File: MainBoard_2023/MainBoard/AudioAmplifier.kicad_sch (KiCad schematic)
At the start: 0 parts

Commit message: アンプ回路
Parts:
- added C? (x7): 1μ, symbol Device:C_Small
- added R? (x7): 10k, symbol Device:R_Small
- added R?: 100k, symbol Device:R_Small
- added U?: YDA142, symbol YDA142:YDA142
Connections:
- new net: R?.1, U?.48 (SLEEPN), U?.49 (PROTN)
- new net: C?.1, U?.1 (VREF), U?.4 (GAINA)
- new net +12V: C?.1, C?.1, C?.1, C?.2, C?.2, R?.2, U?.10 (PVDDR), U?.17 (PVDDR), U?.36 (PVDDL), U?.43 (PVDDL), U?.50 (PVDDREG)
- new net +5VD: C?.1, R?.2, R?.2, R?.2, R?.2, R?.2, R?.2, R?.2, U?.21 (MUTEN), U?.51 (REFA), U?.52 (DVDD)
- new net BCLK: U?.26 (SCLK)
- new net BITSEL: R?.1, U?.33 (BITSEL)
- new net DIN: U?.24 (SDIN)
- new net FSSEL: R?.1, U?.32 (FSSEL)
- new net GAIN0: R?.1, U?.29 (GAIN0)
- new net GAIN1: R?.1, U?.30 (GAIN1)
- new net GAIN2: R?.1, U?.31 (GAIN2)
- new net GND: C?.1, C?.1, C?.2, C?.2, C?.2, C?.2, C?.2, U?.13 (PVSSR), U?.14 (PVSSR), U?.18 (PVSSR), U?.19 (PVSSR), U?.2 (AVSS), U?.22 (MONO), U?.23 (DVSS), U?.3 (VSSBGR), U?.34 (PVSSL), U?.35 (PVSSL), U?.39 (PVSSL), U?.40 (PVSSL), U?.44 (PVSSL), U?.45 (PVSSL), U?.8 (PVSSR), U?.9 (PVSSR)
- new net LRCLK: U?.25 (LRCLK)
- new net MODE0: R?.1, U?.27 (MODE0)
- new net MODE1: R?.1, U?.28 (MODE1)
- new net SP_OUTM_L: U?.37 (OUTML), U?.38 (OUTML)
- new net SP_OUTM_R: U?.15 (OUTMR), U?.16 (OUTMR)
- new net SP_OUTP_L: U?.41 (OUTPL), U?.42 (OUTPL)
- new net SP_OUTP_R: U?.11 (OUTPR), U?.12 (OUTPR)
- no-connect marks 0 -> 6

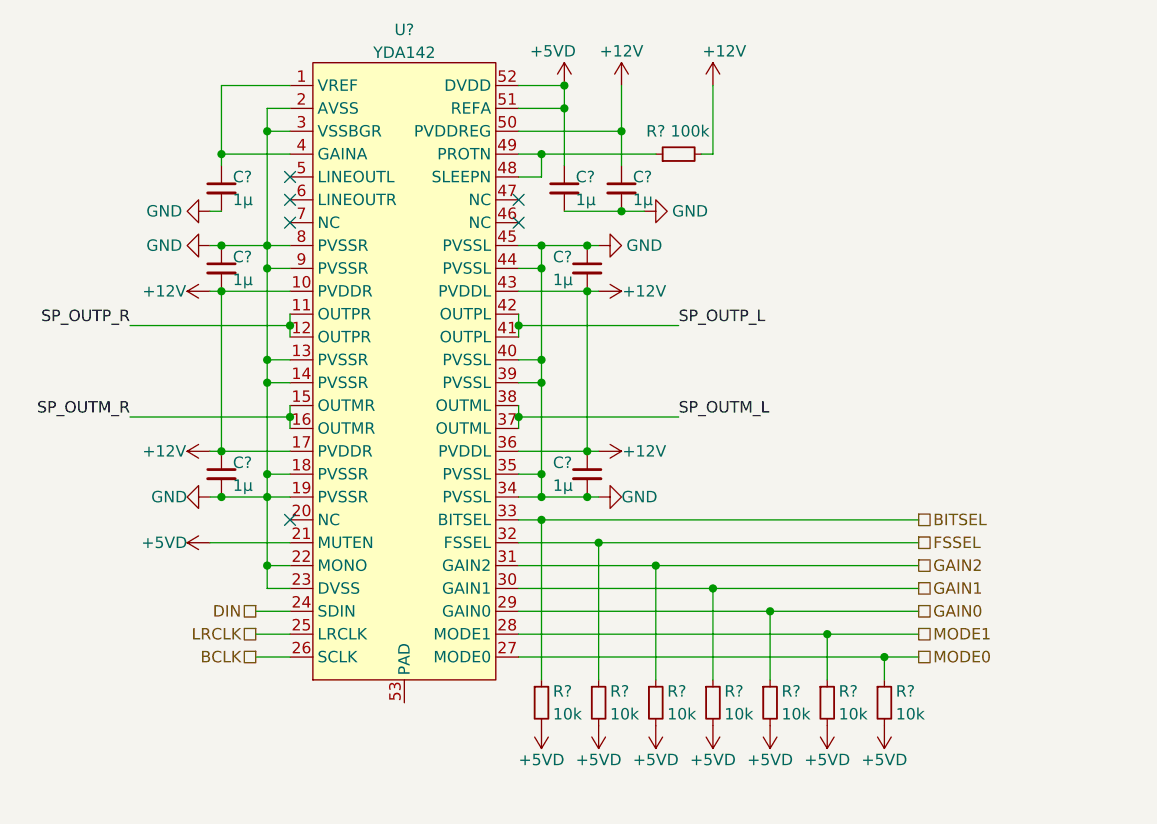
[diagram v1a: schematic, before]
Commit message: 回路だいたい完成
電解コンデンサのシンボルとフットプリントをkicad付属のものにする
ADCのピンと、SPIのOLEDのピンを共用にする
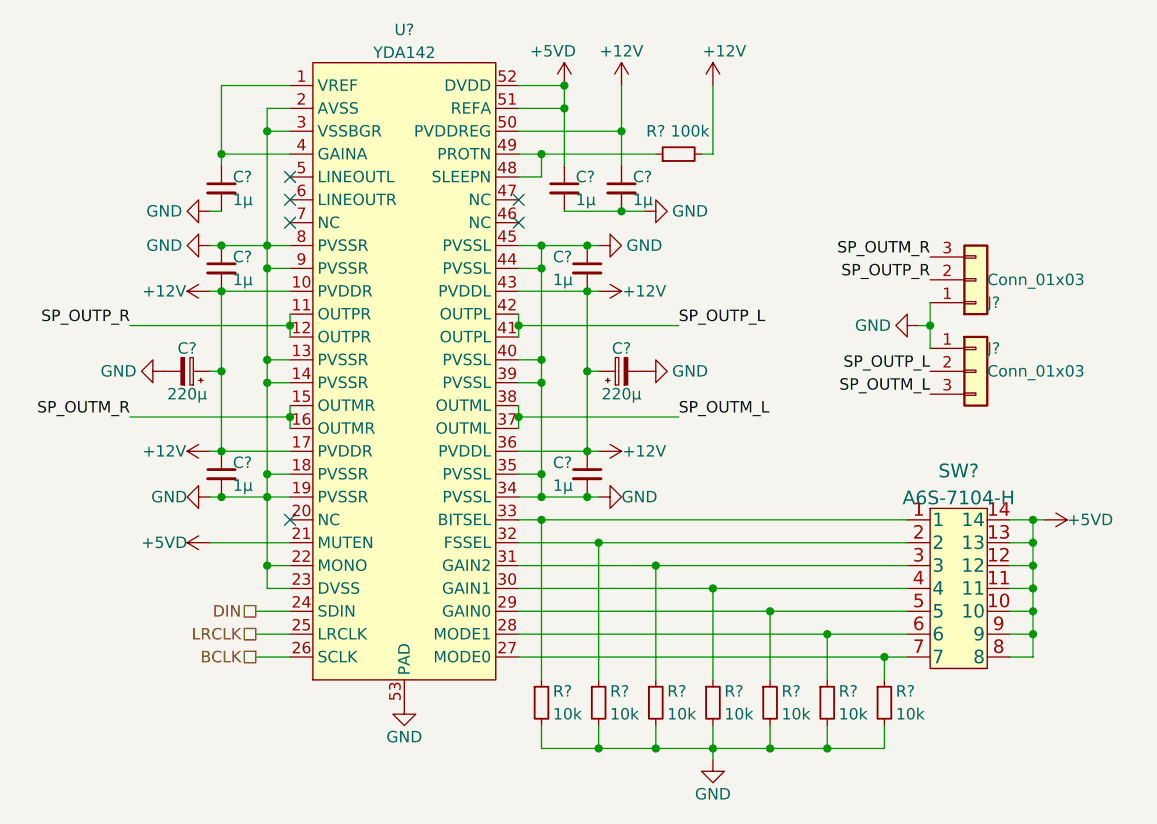
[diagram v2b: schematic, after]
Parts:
- added C? (x2): 220μ, symbol Device:C_Polarized_Small
- added J? (x2): Conn_01x03, symbol Connector_Generic:Conn_01x03
- added SW?: A6S-7104-H, SW_A6S-7104-H_OMR, symbol A6S-7104-H:A6S-7104-H
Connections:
- net +12V: now also C?.1, C?.1
- net +5VD: now also SW?.10, SW?.11, SW?.12, SW?.13, SW?.14, SW?.8, SW?.9; no longer R?.2, R?.2, R?.2, R?.2, R?.2, R?.2, R?.2
- net GND: now also R?.2, R?.2, R?.2, R?.2, R?.2, R?.2, R?.2, U?.53 (PAD), C?.2, C?.2, J?.1 (Pin_1), J?.1 (Pin_1)
- net SP_OUTM_L: now also J?.3 (Pin_3)
- net SP_OUTM_R: now also J?.3 (Pin_3)
- net SP_OUTP_L: now also J?.2 (Pin_2)
- net SP_OUTP_R: now also J?.2 (Pin_2)
- net BITSEL: no longer names the net of R?.1, U?.33 (BITSEL)
- net BITSEL: now also SW?.1
- net FSSEL: no longer names the net of R?.1, U?.32 (FSSEL)
- net FSSEL: now also SW?.2
- net GAIN0: no longer names the net of R?.1, U?.29 (GAIN0)
- net GAIN0: now also SW?.5
- net GAIN1: no longer names the net of R?.1, U?.30 (GAIN1)
- net GAIN1: now also SW?.4
- net GAIN2: no longer names the net of R?.1, U?.31 (GAIN2)
- net GAIN2: now also SW?.3
- net MODE0: no longer names the net of R?.1, U?.27 (MODE0)
- net MODE0: now also SW?.7
- net MODE1: no longer names the net of R?.1, U?.28 (MODE1)
- net MODE1: now also SW?.6

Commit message: ERC通った
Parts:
- gave numbers to parts that had none: 21

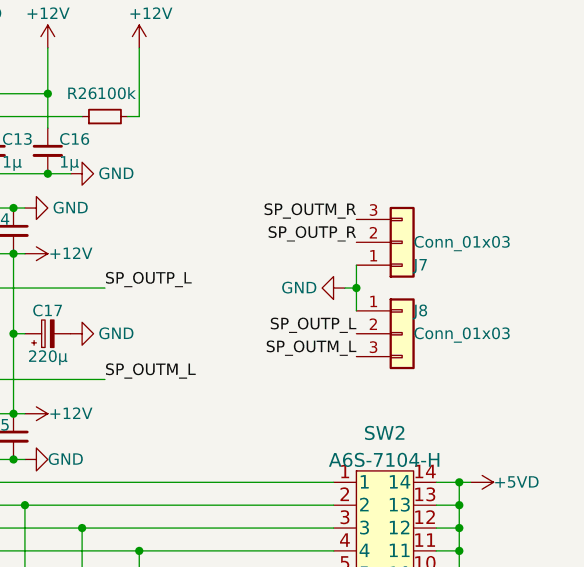
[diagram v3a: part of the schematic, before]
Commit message: フットプリントをすべて割り当て
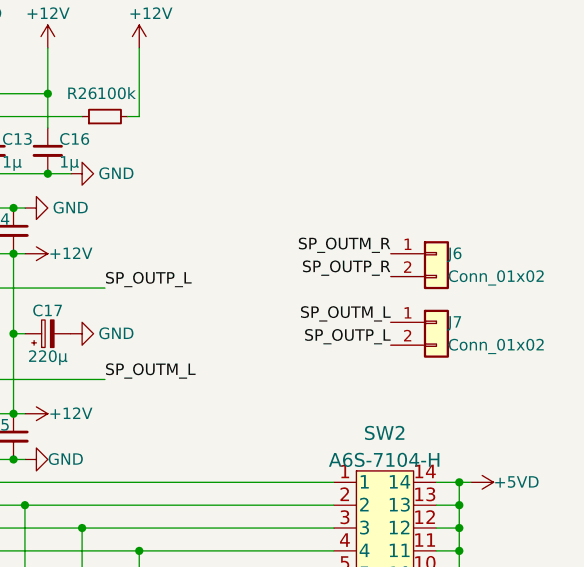
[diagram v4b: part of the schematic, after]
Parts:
- removed J7, J8: Conn_01x03, symbol Connector_Generic:Conn_01x03
- added J6, J7: Conn_01x02, B02B-PASK-1:B02B-PASK-1, symbol Connector_Generic:Conn_01x02
- C10, C11, C12, C13, C14, C15, C16: footprint (none) -> Capacitor_SMD:C_0603_1608Metric_Pad1.08x0.95mm_HandSolder
- C17, C9: footprint (none) -> Capacitor_THT:CP_Radial_D12.5mm_P5.00mm
- R23, R24, R25, R26, R27, R28, R29, R30: footprint (none) -> Resistor_SMD:R_0603_1608Metric_Pad0.98x0.95mm_HandSolder
- SW2: footprint SW_A6S-7104-H_OMR -> A6S-7104-H:A6S-7104-H
- U6: footprint (none) -> YDA142:YDA142
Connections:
- net SP_OUTM_L: now also J7.1 (Pin_1)
- net SP_OUTM_R: now also J6.1 (Pin_1)
- net SP_OUTP_L: now also J7.2 (Pin_2)
- net SP_OUTP_R: now also J6.2 (Pin_2)

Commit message: 部品配置中
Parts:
- J6, J7: footprint B02B-PASK-1:B02B-PASK-1 -> Connector_JST:JST_XA_S02B-XASK-1_1x02_P2.50mm_Horizontal
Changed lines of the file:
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@@
       (effects (font (size 1.27 1.27)) (justify left))
     )
-    (property "Footprint" "B02B-PASK-1:B02B-PASK-1" (id 2) (at 170.18 74.93 0)
+    (property "Footprint" "Connector_JST:JST_XA_S02B-XASK-1_1x02_P2.50mm_Horizontal" (id 2) (at 170.18 74.93 0)
       (effects (font (size 1.27 1.27)) hide)
     )
@@
       (effects (font (size 1.27 1.27)) (justify left))
     )
-    (property "Footprint" "B02B-PASK-1:B02B-PASK-1" (id 2) (at 170.18 67.31 0)
-      (effects (font (size 1.27 1.27)) hide)
-    )
+    (property "Footprint" "Connector_JST:JST_XA_S02B-XASK-1_1x02_P2.50mm_Horizontal" (id 2) (at 170.18 67.31 0)
+      (effects (font (size 1.27 1.27)) hide)
+    )

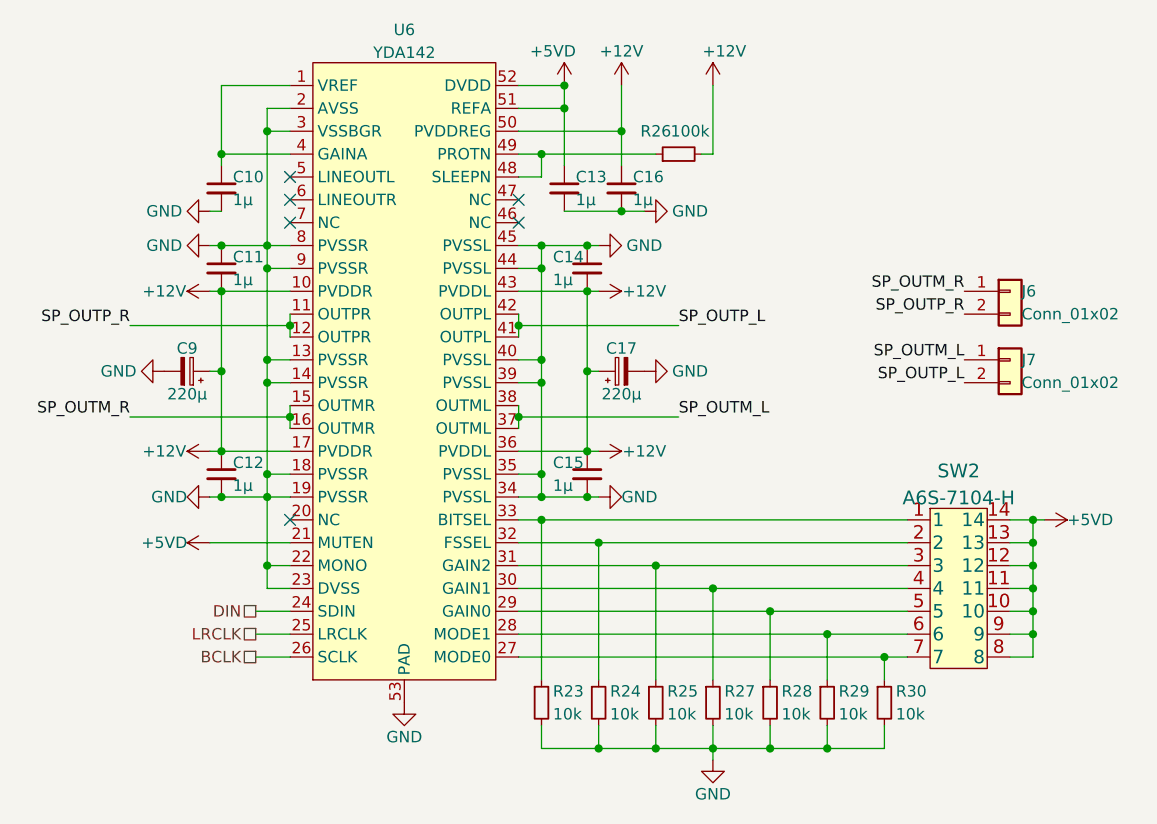
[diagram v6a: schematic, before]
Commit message: 回路図とPCBを変更
RJコネクタに変更
秋月のBNO055に変更
気圧センサのフットプリントを変更
ブロックタイプエミフィルのパッドを縮小
外形と取り付け穴を設定
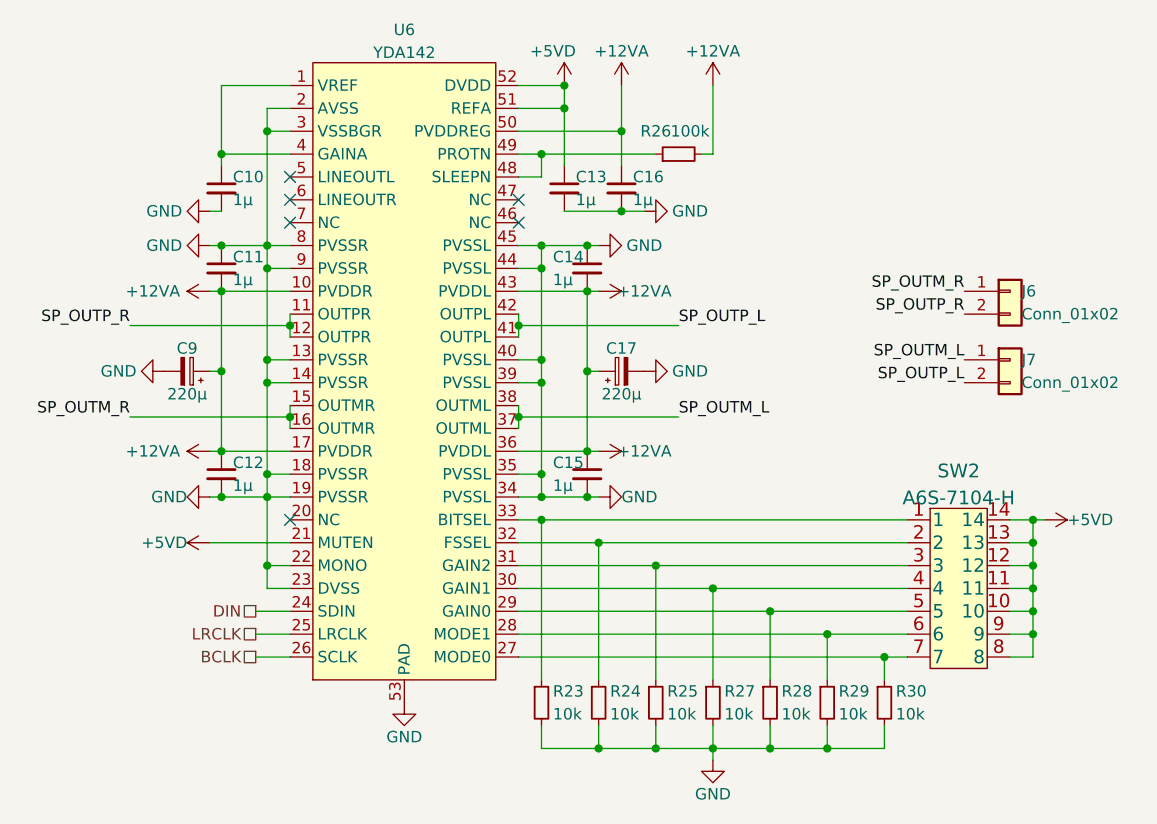
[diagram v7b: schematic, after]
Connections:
- net +12V renamed +12VA

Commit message: シルクを整えた
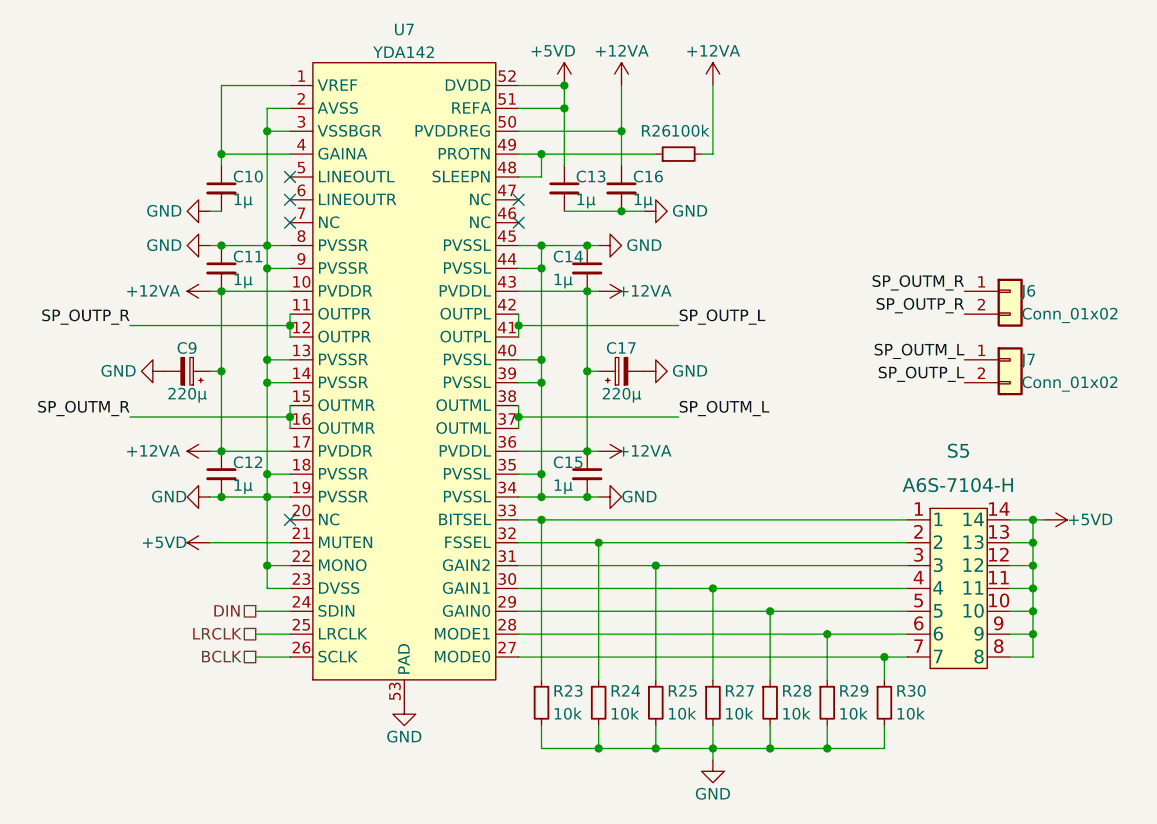
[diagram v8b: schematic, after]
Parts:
- renumbered SW2 to S5, U6 to U7
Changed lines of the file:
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@@
   (symbol (lib_id "A6S-7104-H:A6S-7104-H") (at 158.75 92.71 0) (unit 1)
     (in_bom yes) (on_board yes) (fields_autoplaced)
-    (property "Reference" "SW2" (id 0) (at 164.465 87.2797 0)
+    (property "Reference" "S5" (id 0) (at 164.465 85.09 0)
       (effects (font (size 1.524 1.524)))
     )
-    (property "Value" "A6S-7104-H" (id 1) (at 164.465 90.2731 0)
+    (property "Value" "A6S-7104-H" (id 1) (at 164.465 88.9 0)
       (effects (font (size 1.524 1.524)))
     )
@@
   (symbol (lib_id "YDA142:YDA142") (at 90.17 44.45 0) (unit 1)
     (in_bom yes) (on_board yes) (fields_autoplaced)
-    (property "Reference" "U6" (id 0) (at 102.87 38.261 0))
+    (property "Reference" "U7" (id 0) (at 102.87 38.261 0))
     (property "Value" "YDA142" (id 1) (at 102.87 40.7979 0))
     (property "Footprint" "YDA142:YDA142" (id 2) (at 90.17 85.09 0)
